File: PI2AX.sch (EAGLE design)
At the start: 5 parts, among them IC1 SN74LVC2G241

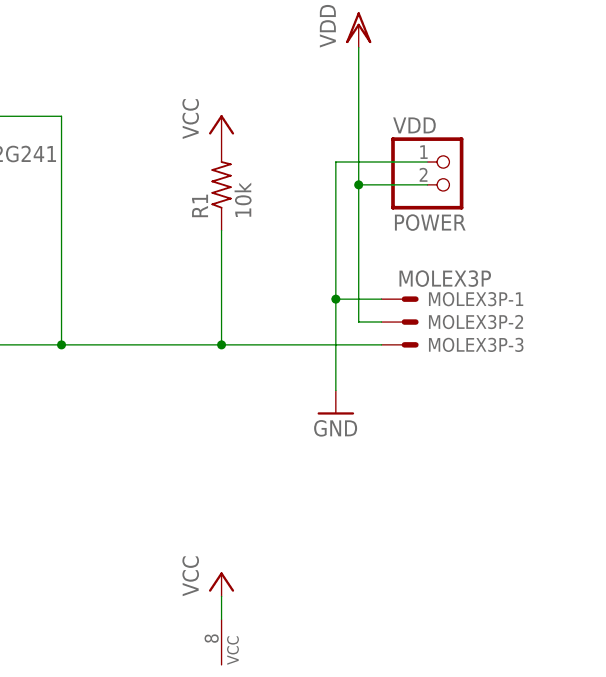
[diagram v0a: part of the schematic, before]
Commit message: revised v1.1, molex connector fixed
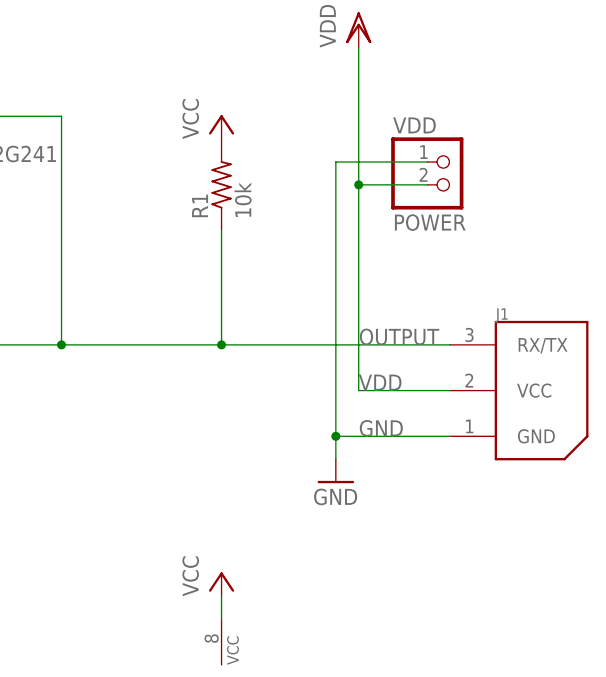
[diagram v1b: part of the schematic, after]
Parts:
- removed MOLEX3P: MOLEX3P, con-molex:53047-03
- added J1: 22-03-5035, molex:22-03-5035
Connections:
- net GND: now also J1.GND; no longer MOLEX3P-1.S
- net OUTPUT: now also J1.RX/TX; no longer MOLEX3P-3.S
- net VDD: now also J1.VCC; no longer MOLEX3P-2.S
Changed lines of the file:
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@@
 <setting verticaltext="up"/>
 </settings>
-<grid distance="0.1" unitdist="inch" unit="inch" style="lines" multiple="1" display="no" altdistance="0.01" altunitdist="inch" altunit="inch"/>
+<grid distance="0.1" unitdist="inch" unit="inch" style="dots" multiple="1" display="yes" altdistance="0.01" altunitdist="inch" altunit="inch"/>
 <layers>
 <layer number="1" name="Top" color="4" fill="1" visible="no" active="no"/>
@@
 <layer number="51" name="tDocu" color="7" fill="1" visible="no" active="no"/>
 <layer number="52" name="bDocu" color="7" fill="1" visible="no" active="no"/>
+<layer number="53" name="tGND_GNDA" color="7" fill="9" visible="no" active="no"/>
+<layer number="54" name="bGND_GNDA" color="1" fill="9" visible="no" active="no"/>
+<layer number="56" name="wert" color="7" fill="1" visible="no" active="no"/>
 <layer number="90" name="Modules" color="5" fill="1" visible="yes" active="yes"/>
 <layer number="91" name="Nets" color="2" fill="1" visible="yes" active="yes"/>
@@
 <layer number="98" name="Guide" color="6" fill="1" visible="yes" active="yes"/>
 <layer number="99" name="SpiceOrder" color="5" fill="1" visible="yes" active="yes"/>
+<layer number="100" name="Muster" color="7" fill="1" visible="no" active="no"/>
+<layer number="101" name="Patch_Top" color="12" fill="4" visible="no" active="yes"/>
+<layer number="102" name="Vscore" color="7" fill="1" visible="no" active="yes"/>
+<layer number="104" name="Name" color="7" fill="1" visible="no" active="yes"/>
+<layer number="105" name="Beschreib" color="9" fill="1" visible="no" active="no"/>
+<layer number="106" name="BGA-Top" color="4" fill="1" visible="no" active="no"/>
+<layer number="107" name="BD-Top" color="5" fill="1" visible="no" active="no"/>
+<layer number="116" name="Patch_BOT" color="9" fill="4" visible="no" active="yes"/>
+<layer number="121" name="_tsilk" color="7" fill="1" visible="no" active="yes"/>
+<layer number="122" name="_bsilk" color="7" fill="1" visible="no" active="yes"/>
+<layer number="151" name="HeatSink" color="7" fill="1" visible="no" active="yes"/>
+<layer number="200" name="200bmp" color="1" fill="10" visible="no" active="yes"/>
+<layer number="201" name="201bmp" color="2" fill="10" visible="no" active="yes"/>
+<layer number="202" name="202bmp" color="3" fill="10" visible="no" active="yes"/>
+<layer number="203" name="203bmp" color="4" fill="10" visible="no" active="yes"/>
+<layer number="204" name="204bmp" color="5" fill="10" visible="no" active="yes"/>
+<layer number="205" name="205bmp" color="6" fill="10" visible="no" active="yes"/>
+<layer number="206" name="206bmp" color="7" fill="10" visible="no" active="yes"/>
+<layer number="207" name="207bmp" color="8" fill="10" visible="no" active="yes"/>
+<layer number="208" name="208bmp" color="9" fill="10" visible="no" active="yes"/>
+<layer number="250" name="Descript" color="3" fill="1" visible="no" active="no"/>
+<layer number="251" name="SMDround" color="12" fill="11" visible="no" active="no"/>
+<layer number="254" name="cooling" color="7" fill="1" visible="no" active="yes"/>
 </layers>
 <schematic xreflabel="%F%N/%S.%C%R" xrefpart="/%S.%C%R">
@@
 <parts>
 <part name="R1" library="resistor" deviceset="R-US_" device="R0805" value="10k"/>
-<part name="MOLEX3P" library="con-molex" deviceset="53?-03" device="047" value="MOLEX3P"/>
 <part name="P+1" library="supply1" deviceset="VCC" device=""/>
 <part name="P+2" library="supply1" deviceset="VCC" device=""/>
@@
 <part name="VDD" library="pinhead" deviceset="PINHD-1X2" device="" value="POWER"/>
 <part name="IC1" library="74xx-little-de" deviceset="SN74LVC2G241" device=""/>
+<part name="J1" library="molex" deviceset="22-03-5035" device=""/>
 </parts>
 <sheets>
@@
 <instances>
 <instance part="R1" gate="G$1" x="96.52" y="60.96" rot="R90"/>
-<instance part="MOLEX3P" gate="-1" x="116.84" y="48.26"/>
-<instance part="MOLEX3P" gate="-2" x="116.84" y="45.72"/>
-<instance part="MOLEX3P" gate="-3" x="116.84" y="43.18"/>
 <instance part="P+1" gate="VCC" x="96.52" y="17.78"/>
 <instance part="P+2" gate="VCC" x="96.52" y="68.58"/>
@@
 <instance part="GND1" gate="1" x="-7.62" y="30.48"/>
 <instance part="GND2" gate="1" x="96.52" y="-7.62"/>
-<instance part="GND3" gate="1" x="109.22" y="35.56"/>
+<instance part="GND3" gate="1" x="109.22" y="27.94"/>
 <instance part="GND4" gate="1" x="12.7" y="30.48"/>
 <instance part="JP1" gate="A" x="2.54" y="48.26"/>
@@
 <instance part="IC1" gate="B" x="58.42" y="68.58"/>
 <instance part="IC1" gate="P" x="96.52" y="5.08"/>
+<instance part="J1" gate="G$1" x="132.08" y="38.1"/>
 </instances>
 <busses>
@@
 <segment>
 <wire x1="78.74" y1="43.18" x2="78.74" y2="68.58" width="0.1524" layer="91"/>
-<pinref part="MOLEX3P" gate="-3" pin="S"/>
-<wire x1="114.3" y1="43.18" x2="96.52" y2="43.18" width="0.1524" layer="91"/>
 <pinref part="R1" gate="G$1" pin="1"/>
 <wire x1="96.52" y1="43.18" x2="78.74" y2="43.18" width="0.1524" layer="91"/>
 <wire x1="96.52" y1="55.88" x2="96.52" y2="43.18" width="0.1524" layer="91"/>
-<junction x="96.52" y="43.18"/>
 <pinref part="IC1" gate="A" pin="I"/>
 <wire x1="68.58" y1="43.18" x2="78.74" y2="43.18" width="0.1524" layer="91"/>
@@
 <pinref part="IC1" gate="B" pin="O"/>
 <wire x1="66.04" y1="68.58" x2="78.74" y2="68.58" width="0.1524" layer="91"/>
+<pinref part="J1" gate="G$1" pin="RX/TX"/>
+<wire x1="121.92" y1="43.18" x2="96.52" y2="43.18" width="0.1524" layer="91"/>
+<junction x="96.52" y="43.18"/>
+<label x="111.76" y="43.18" size="1.778" layer="95"/>
 </segment>
 </net>
@@
 <segment>
 <pinref part="GND3" gate="1" pin="GND"/>
-<wire x1="109.22" y1="48.26" x2="109.22" y2="38.1" width="0.1524" layer="91"/>
-<pinref part="MOLEX3P" gate="-1" pin="S"/>
-<wire x1="114.3" y1="48.26" x2="109.22" y2="48.26" width="0.1524" layer="91"/>
+<wire x1="109.22" y1="33.02" x2="109.22" y2="30.48" width="0.1524" layer="91"/>
 <pinref part="VDD" gate="G$1" pin="1"/>
 <wire x1="119.38" y1="63.5" x2="109.22" y2="63.5" width="0.1524" layer="91"/>
-<wire x1="109.22" y1="63.5" x2="109.22" y2="48.26" width="0.1524" layer="91"/>
-<junction x="109.22" y="48.26"/>
+<wire x1="109.22" y1="63.5" x2="109.22" y2="33.02" width="0.1524" layer="91"/>
+<pinref part="J1" gate="G$1" pin="GND"/>
+<wire x1="121.92" y1="33.02" x2="109.22" y2="33.02" width="0.1524" layer="91"/>
+<junction x="109.22" y="33.02"/>
+<label x="111.76" y="33.02" size="1.778" layer="95"/>
 </segment>
 <segment>
@@
 <wire x1="111.76" y1="60.96" x2="111.76" y2="76.2" width="0.1524" layer="91"/>
 <wire x1="119.38" y1="60.96" x2="111.76" y2="60.96" width="0.1524" layer="91"/>
-<pinref part="MOLEX3P" gate="-2" pin="S"/>
-<wire x1="114.3" y1="45.72" x2="111.76" y2="45.72" width="0.1524" layer="91"/>
-<wire x1="111.76" y1="45.72" x2="111.76" y2="60.96" width="0.1524" layer="91"/>
+<pinref part="J1" gate="G$1" pin="VCC"/>
+<wire x1="121.92" y1="38.1" x2="111.76" y2="38.1" width="0.1524" layer="91"/>
+<wire x1="111.76" y1="38.1" x2="111.76" y2="60.96" width="0.1524" layer="91"/>
 <junction x="111.76" y="60.96"/>
-</segment>
-</net>
+<label x="111.76" y="38.1" size="1.778" layer="95"/>
+</segment>
+</net>
